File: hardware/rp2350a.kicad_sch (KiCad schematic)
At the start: 32 parts, among them Q26 AP1606, U10 RP2354A, X1 12MHz

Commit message: Preserve owner schematic and board before final design review
Snapshot of the saved working design supplied for review.
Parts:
- removed C134: 4.7uF, lib:C_0201_0603Metric_L, symbol Device:C
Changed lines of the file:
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@@
 	)
 	(junction
-		(at 256.54 208.28)
-		(diameter 0)
-		(color 0 0 0 0)
-	)
-	(junction
 		(at 125.73 171.45)
 		(diameter 0)
@@
 	(wire
 		(pts
-			(xy 256.54 182.88) (xy 256.54 208.28)
-		)
-		(stroke
-			(width 0)
-			(type default)
-		)
-	)
-	(wire
-		(pts
 			(xy 138.43 107.95) (xy 143.51 107.95)
 		)
@@
 	)
 	(symbol
-		(lib_id "Device:C")
-		(at 256.54 179.07 0)
-		(unit 1)
-		(body_style 1)
-		(exclude_from_sim no)
-		(in_bom yes)
-		(on_board yes)
-		(in_pos_files yes)
-		(dnp no)
-		(property "Reference" "C134"
-			(at 260.35 177.7999 0)
-			(show_name no)
-			(do_not_autoplace no)
-			(effects
-				(font
-					(size 1.27 1.27)
-				)
-				(justify left)
-			)
-		)
-		(property "Value" "4.7uF"
-			(at 260.35 180.3399 0)
-			(show_name no)
-			(do_not_autoplace no)
-			(effects
-				(font
-					(size 1.27 1.27)
-				)
-				(justify left)
-			)
-		)
-		(property "Footprint" "lib:C_0201_0603Metric_L"
-			(at 256.54 179.07 0)
-			(hide yes)
-			(show_name no)
-			(do_not_autoplace no)
-			(effects
-				(font
-					(size 1.27 1.27)
-				)
-			)
-		)
-		(property "Datasheet" ""
-			(at 256.54 179.07 0)
-			(hide yes)
-			(show_name no)
-			(do_not_autoplace no)
-			(effects
-				(font
-					(size 1.27 1.27)
-				)
-			)
-		)
-		(property "Description" "Unpolarized capacitor"
-			(at 256.54 179.07 0)
-			(hide yes)
-			(show_name no)
-			(do_not_autoplace no)
-			(effects
-				(font
-					(size 1.27 1.27)
-				)
-			)
-		)
-		(property "LCSC" "C335103"
-			(at 256.54 179.07 0)
-			(hide yes)
-			(show_name no)
-			(do_not_autoplace no)
-			(effects
-				(font
-					(size 1.27 1.27)
-				)
-			)
-		)
-		(property "MPN" "GRM035R60J475ME15D"
-			(at 256.54 179.07 0)
-			(hide yes)
-			(show_name no)
-			(do_not_autoplace no)
-			(effects
-				(font
-					(size 1.27 1.27)
-				)
-			)
-		)
-		(property "Manufacturer" "Murata"
-			(at 256.54 179.07 0)
-			(hide yes)
-			(show_name no)
-			(do_not_autoplace no)
-			(effects
-				(font
-					(size 1.27 1.27)
-				)
-			)
-		)
-		(pin "1"
-		)
-		(pin "2"
-		)
-		(instances
-			(project "OpenAIO-Whoop"
-				(path "/2c3a7206-1e66-4d43-a02f-491225e20dd6/df951d63-8e6a-5171-a7c4-15005f1245fb"
-					(reference "C134")
-					(unit 1)
-				)
-			)
-		)
-	)
-	(symbol
 		(lib_id "power:+3.3V")
 		(at 198.12 46.99 0)
@@
 					(unit 1)
 				)
-			)
-		)
-	)
-	(symbol
-		(lib_id "power:+3.3V")
-		(at 256.54 175.26 0)
-		(unit 1)
-		(body_style 1)
-		(exclude_from_sim no)
-		(in_bom no)
-		(on_board yes)
-		(in_pos_files no)
-		(dnp no)
-		(property "Reference" "#PWR112"
-			(at 256.54 179.07 0)
-			(hide yes)
-			(show_name no)
-			(do_not_autoplace no)
-			(effects
-				(font
-					(size 1.27 1.27)
-				)
-			)
-		)
-		(property "Value" "+1.1V"
-			(at 256.54 171.704 0)
-			(show_name no)
-			(do_not_autoplace no)
-			(effects
-				(font
-					(size 1.27 1.27)
-				)
-			)
-		)
-		(property "Footprint" ""
-			(at 256.54 175.26 0)
-			(hide yes)
-			(show_name no)
-			(do_not_autoplace no)
-			(effects
-				(font
-					(size 1.27 1.27)
-				)
-			)
-		)
-		(property "Datasheet" ""
-			(at 256.54 175.26 0)
-			(hide yes)
-			(show_name no)
-			(do_not_autoplace no)
-			(effects
-				(font
-					(size 1.27 1.27)
-				)
-			)
-		)
-		(property "Description" "Power symbol creates a global label with name \"+1.1V\""
-			(at 256.54 175.26 0)
-			(hide yes)
-			(show_name no)
-			(do_not_autoplace no)
-			(effects
-				(font
-					(size 1.27 1.27)
-				)
-			)
-		)
-		(pin "1"
-		)
-		(instances
-			(project "OpenAIO-Whoop"
-				(path "/2c3a7206-1e66-4d43-a02f-491225e20dd6/df951d63-8e6a-5171-a7c4-15005f1245fb"
-					(reference "#PWR112")
-					(unit 1)
-				)

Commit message: Correct Whoop schematic and prepare component library for routing
Add local BMI270 bypassing, improve regulator capacitance margin, isolate
bidirectional DShot supply domains, and correct PA reference accuracy.
Remove Q28/R11 with matching firmware polarity and retain the proven
OpenFC-Lite OSD topology. Correct the receiver LED bypass rail.

Synchronize PCB connectivity, verify component pins and land patterns,
and provide firmware bindings plus placement/layer guidance. Replace stale
manual BOM and interface plans with schematic-derived exports.

Validation: ERC 0, seven netlist checks, 48 footprint checks, 22 rule
behavior cases, and PCB schematic parity 0. The parked PCB retains layout
DRC findings and 499 unconnected items; no manufacturing or flight release.
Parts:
- added C143, C144: 100nF, lib:C_0201_0603Metric_L, symbol Device:C
- added U24: FXMAR2104UMX, lib:Onsemi_UMLP-12_1.8x1.8mm_P0.4mm_FXMAR2104, symbol lib:FXMAR2104UMX
- C52: value 100nF -> 4.7uF; LCSC C181047 -> C335103; MPN GRM033C81E104KE14D -> GRM035R60J475ME15D
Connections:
- net +3.3V: now also C143.1, U24.2 (VCCA), U24.8 (OE)
- net +BATT: now also C144.1, U24.1 (VCCB)
- net GND: now also C143.2, C144.2, U24.7 (GND)
- net MOTOR1: now also U24.12 (B0); no longer U10.7 (GPIO4)
- net MOTOR2: now also U24.11 (B1); no longer U10.9 (GPIO6)
- net MOTOR3: now also U24.10 (B2); no longer U10.29 (GPIO18)
- net MOTOR4: now also U24.9 (B3); no longer U10.32 (GPIO20)
- net U10_USB_DM renamed U10_USB_D_N
- net U10_USB_DP renamed U10_USB_D_P
- new net MOTOR1_FC: U10.7 (GPIO4), U24.3 (A0)
- new net MOTOR2_FC: U10.9 (GPIO6), U24.4 (A1)
- new net MOTOR3_FC: U10.29 (GPIO18), U24.5 (A2)
- new net MOTOR4_FC: U10.32 (GPIO20), U24.6 (A3)
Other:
- note added: "DShot: supply translation and isolation"

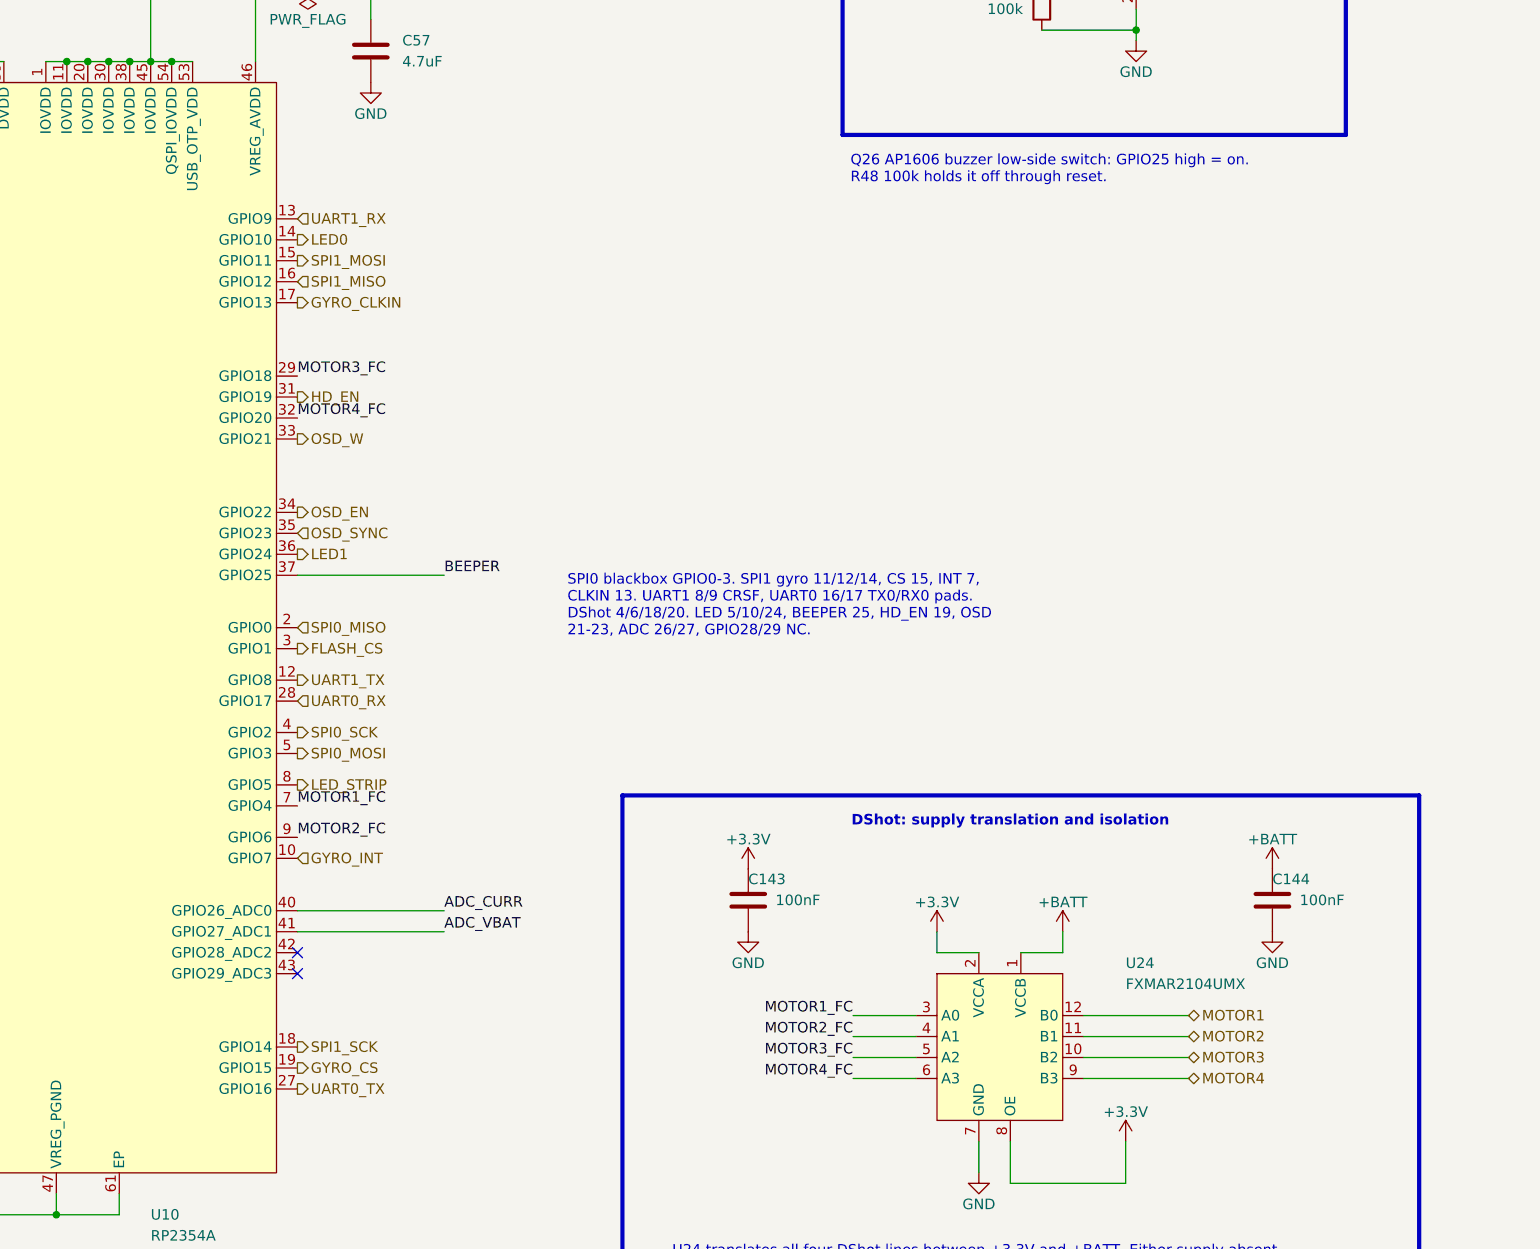
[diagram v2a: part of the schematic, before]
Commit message: Group RP2354A interfaces around the placed peripherals
Map motors 1-4 to GPIO7/6/5/4 for U24 north-side fanout, move gyro INT
to GPIO10, and put CRSF UART1 on GPIO24/25 beside the ESP32. Keep the
gyro SPI pad order, flash, OSD, ADC and dedicated system pins. Move the
status LEDs, strip and beeper to the released pins.

Synchronize the target, project library, PCB nets and schematic print; add
a schematic-to-firmware IO check with mux and PIO constraints. Remove eight
stale PCB footprints already absent from the owner schematic. Preserve all
retained placement and copper geometry.

Validation: 28 GPIOs match, 7 netlist checks and 22 rule behavior cases pass,
Betaflight builds, independent circuit/PCB review passes. ERC retains four
owner warnings; parity is zero. Board layout has 282 DRC findings and
499 unconnected items. This is not a hardware-tested release.
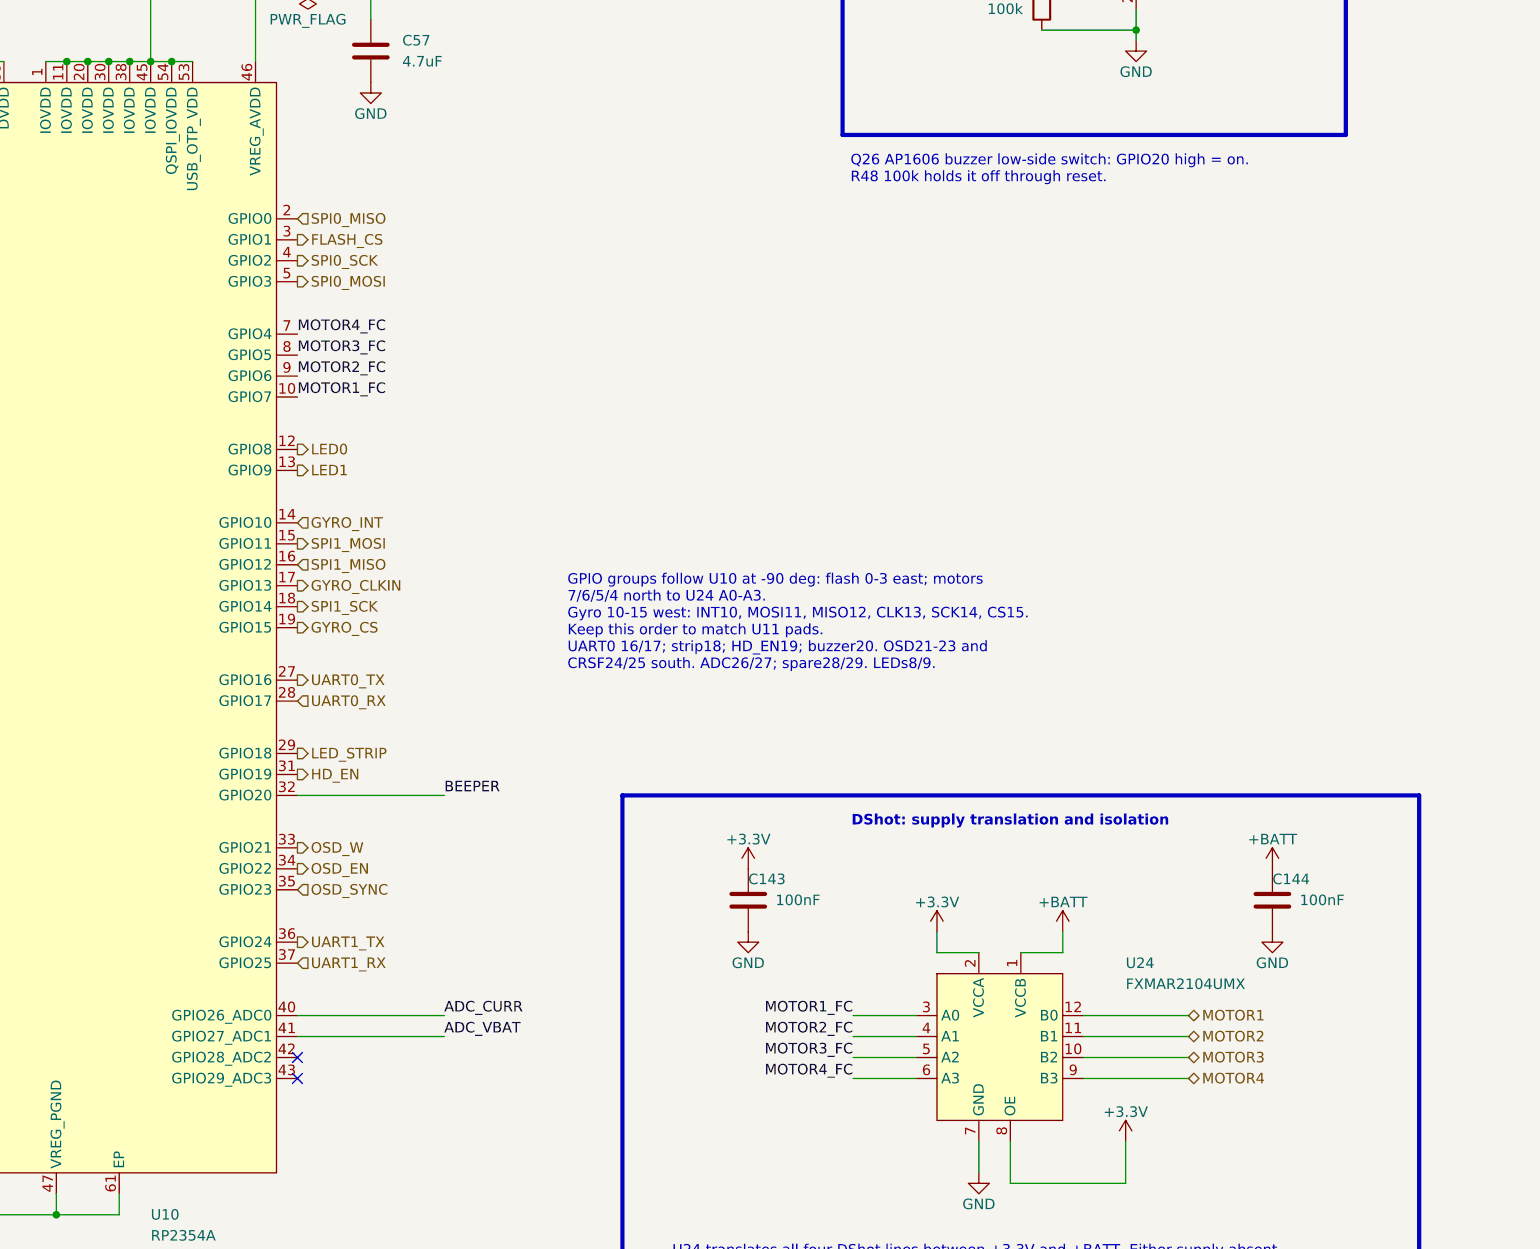
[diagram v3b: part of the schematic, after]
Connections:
- net BEEPER: now also U10.32 (GPIO20); no longer U10.37 (GPIO25)
- net GYRO_INT: now also U10.14 (GPIO10); no longer U10.10 (GPIO7)
- net LED0: now also U10.12 (GPIO8); no longer U10.14 (GPIO10)
- net LED1: now also U10.13 (GPIO9); no longer U10.36 (GPIO24)
- net LED_STRIP: now also U10.29 (GPIO18); no longer U10.8 (GPIO5)
- net MOTOR1_FC: now also U10.10 (GPIO7); no longer U10.7 (GPIO4)
- net MOTOR3_FC: now also U10.8 (GPIO5); no longer U10.29 (GPIO18)
- net MOTOR4_FC: now also U10.7 (GPIO4); no longer U10.32 (GPIO20)
- net UART1_RX: now also U10.37 (GPIO25); no longer U10.13 (GPIO9)
- net UART1_TX: now also U10.36 (GPIO24); no longer U10.12 (GPIO8)
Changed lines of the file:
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@@
 		)
 	)
-	(text_box "SPI0 blackbox GPIO0-3. SPI1 gyro 11/12/14, CS 15, INT 7, CLKIN 13. UART1 8/9 CRSF, UART0 16/17 TX0/RX0 pads.\nDShot 4/6/18/20. LED 5/10/24, BEEPER 25, HD_EN 19, OSD 21-23, ADC 26/27, GPIO28/29 NC."
+	(text_box "GPIO groups follow U10 at -90 deg: flash 0-3 east; motors 7/6/5/4 north to U24 A0-A3.\nGyro 10-15 west: INT10, MOSI11, MISO12, CLK13, SCK14, CS15. Keep this order to match U11 pads.\nUART0 16/17; strip18; HD_EN19; buzzer20. OSD21-23 and CRSF24/25 south. ADC26/27; spare28/29. LEDs8/9."
 		(exclude_from_sim no)
 		(at 353.06 129.54 0)
@@
 		)
 	)
-	(text_box "Q26 AP1606 buzzer low-side switch: GPIO25 high = on. R48 100k holds it off through reset."
+	(text_box "Q26 AP1606 buzzer low-side switch: GPIO20 high = on. R48 100k holds it off through reset."
 		(exclude_from_sim no)
 		(at 387.35 78.74 0)
@@
 	)
 	(no_connect
-		(at 321.31 179.07)
+		(at 321.31 191.77)
 	)
 	(no_connect
-		(at 321.31 176.53)
+		(at 321.31 189.23)
 	)
 	(no_connect
@@
 	(wire
 		(pts
-			(xy 321.31 130.81) (xy 339.09 130.81)
+			(xy 321.31 157.48) (xy 339.09 157.48)
 		)
 		(stroke
@@
 	(wire
 		(pts
-			(xy 321.31 173.99) (xy 339.09 173.99)
+			(xy 321.31 186.69) (xy 339.09 186.69)
 		)
 		(stroke
@@
 	(wire
 		(pts
-			(xy 321.31 171.45) (xy 339.09 171.45)
+			(xy 321.31 184.15) (xy 339.09 184.15)
 		)
 		(stroke
@@
 	)
 	(label "MOTOR1_FC"
-		(at 321.31 158.75 0)
+		(at 321.31 109.22 0)
 		(effects
 			(font
@@
 	)
 	(label "ADC_VBAT"
-		(at 339.09 173.99 0)
+		(at 339.09 186.69 0)
 		(effects
 			(font
@@
 	)
 	(label "MOTOR2_FC"
-		(at 321.31 162.56 0)
+		(at 321.31 106.68 0)
 		(effects
 			(font
@@
 	)
 	(label "MOTOR4_FC"
-		(at 321.31 111.76 0)
+		(at 321.31 101.6 0)
 		(effects
 			(font
@@
 	)
 	(label "ADC_CURR"
-		(at 339.09 171.45 0)
+		(at 339.09 184.15 0)
 		(effects
 			(font
@@
 	)
 	(label "BEEPER"
-		(at 339.09 130.81 0)
+		(at 339.09 157.48 0)
 		(effects
 			(font
@@
 	)
 	(label "MOTOR3_FC"
-		(at 321.31 106.68 0)
+		(at 321.31 104.14 0)
 		(effects
 			(font
@@
 	(hierarchical_label "OSD_SYNC"
 		(shape input)
-		(at 321.31 125.73 0)
+		(at 321.31 168.91 0)
 		(effects
 			(font
@@
 	(hierarchical_label "SPI1_SCK"
 		(shape output)
-		(at 321.31 187.96 0)
+		(at 321.31 134.62 0)
 		(effects
 			(font
@@
 	(hierarchical_label "GYRO_CLKIN"
 		(shape output)
-		(at 321.31 97.79 0)
+		(at 321.31 132.08 0)
 		(effects
 			(font
@@
 	(hierarchical_label "UART1_TX"
 		(shape output)
-		(at 321.31 143.51 0)
+		(at 321.31 175.26 0)
 		(effects
 			(font
@@
 	(hierarchical_label "UART1_RX"
 		(shape input)
-		(at 321.31 87.63 0)
+		(at 321.31 177.8 0)
 		(effects
 			(font
@@
 	(hierarchical_label "UART0_TX"
 		(shape output)
-		(at 321.31 193.04 0)
+		(at 321.31 143.51 0)
 		(effects
 			(font
@@
 	(hierarchical_label "SPI0_MISO"
 		(shape input)
-		(at 321.31 137.16 0)
+		(at 321.31 87.63 0)
 		(effects
 			(font
@@
 	(hierarchical_label "SPI0_MOSI"
 		(shape output)
-		(at 321.31 152.4 0)
+		(at 321.31 95.25 0)
 		(effects
 			(font
@@
 	(hierarchical_label "SPI1_MISO"
 		(shape input)
-		(at 321.31 95.25 0)
+		(at 321.31 129.54 0)
 		(effects
 			(font
@@
 	(hierarchical_label "HD_EN"
 		(shape output)
-		(at 321.31 109.22 0)
+		(at 321.31 154.94 0)
 		(effects
 			(font
@@
 	(hierarchical_label "LED_STRIP"
 		(shape output)
-		(at 321.31 156.21 0)
+		(at 321.31 152.4 0)
 		(effects
 			(font
@@
 	(hierarchical_label "SPI0_SCK"
 		(shape output)
-		(at 321.31 149.86 0)
+		(at 321.31 92.71 0)
 		(effects
 			(font
@@
 	(hierarchical_label "OSD_W"
 		(shape output)
-		(at 321.31 114.3 0)
+		(at 321.31 163.83 0)
 		(effects
 			(font
@@
 	(hierarchical_label "OSD_EN"
 		(shape output)
-		(at 321.31 123.19 0)
+		(at 321.31 166.37 0)
 		(effects
 			(font
@@
 	(hierarchical_label "GYRO_INT"
 		(shape input)
-		(at 321.31 165.1 0)
+		(at 321.31 124.46 0)
 		(effects
 			(font
@@
 	(hierarchical_label "FLASH_CS"
 		(shape output)
-		(at 321.31 139.7 0)
+		(at 321.31 90.17 0)
 		(effects
 			(font
@@
 	(hierarchical_label "LED1"
 		(shape output)
-		(at 321.31 128.27 0)
+		(at 321.31 118.11 0)
 		(effects
 			(font
@@
 	(hierarchical_label "GYRO_CS"
 		(shape output)
-		(at 321.31 190.5 0)
+		(at 321.31 137.16 0)
 		(effects
 			(font
@@
 	(hierarchical_label "LED0"
 		(shape output)
-		(at 321.31 90.17 0)
+		(at 321.31 115.57 0)
 		(effects
 			(font
@@
 	(hierarchical_label "SPI1_MOSI"
 		(shape output)
-		(at 321.31 92.71 0)
-		(effects
-			(font
+		(at 321.31 127 0)
+		(effects
+			(font
